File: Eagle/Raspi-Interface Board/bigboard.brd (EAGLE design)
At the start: 41.9 x 42.9 mm, 25 parts, among them M1 SMALL_SERVO, M2 SMALL_SERVO, M3 SMALL_SERVO, M4 SMALL_SERVO, M5 SMALL_SERVO, U1 ATMEGA328P-AU

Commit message: AVR ISP pins corrected
In the R1 of the board the AVR ISP pins were totally attached to the
wrong. 13 != 3. Double check work done at 4AM next time.
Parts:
- removed IC1, IC2: (no value), RepRapjr:TO92-LINE
- added 3VREG, 5VREG: (no value), SparkFun-Connectors:1X03
- added U$1, U$2: (no value), SparkFun-Aesthetics:FKIT-LOGO_VERY_SMALL
- moved R3 8.13 mm to (11.4, 11.4), turned to 180 degrees
- moved R2 7.18 mm to (11.4, 14.0)
- moved R1 6.35 mm to (11.4, 16.5)
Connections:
- net 3V: now also 3VREG.1; no longer IC2.3
- net 5V: now also 3VREG.3, 5VREG.1; no longer IC1.3, IC2.1
- net A3: now also JP3.4
- net A4: no longer JP3.4
- net ATX: no longer ISP1.1
- net D12: now also ISP1.1
- net D13: now also ISP1.3
- net D3: no longer ISP1.3
- net GND: now also 3VREG.2, 5VREG.2; no longer IC1.2, IC2.2
- net VIN: now also 5VREG.3; no longer IC1.1
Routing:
- net D12: track 42.0 -> 93.9 mm, vias 3 -> 2
- net D11: track 78.2 -> 50.3 mm, vias 1 -> 2
- net D13: track 34.8 -> 59.1 mm, vias 3 -> 1
- net A3: track 0.00 -> 23.2 mm, vias 0 -> 2
- net D3: track 31.9 -> 12.8 mm, vias 2 -> 1
- net ATX: track 38.1 -> 23.3 mm, vias 3 -> 2
- net D9: track 32.2 -> 42.8 mm
- net RRX: track 17.4 -> 9.49 mm
- net ARX: track 36.1 -> 28.3 mm, vias 2 -> 1
- net RESET: track 26.4 -> 33.4 mm
- net A2: track 29.8 -> 24.1 mm, vias 0 -> 2
- net D8: track 47.2 -> 42.5 mm, vias 4 -> 2
- net D10: track 36.1 -> 31.7 mm
- net D7: track 32.5 -> 36.6 mm, vias 1 -> 2
- net GND: track 3.19 -> 0.00 mm, vias 13 -> 2
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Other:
- board text added: "4%"
- board text added: "5/18/14"
- board text added: "R3"
- board text removed: "5/5/14"
- board text removed: "Approved"
- board text removed: "CC BY-SA 4.0"
- board text removed: "R1"

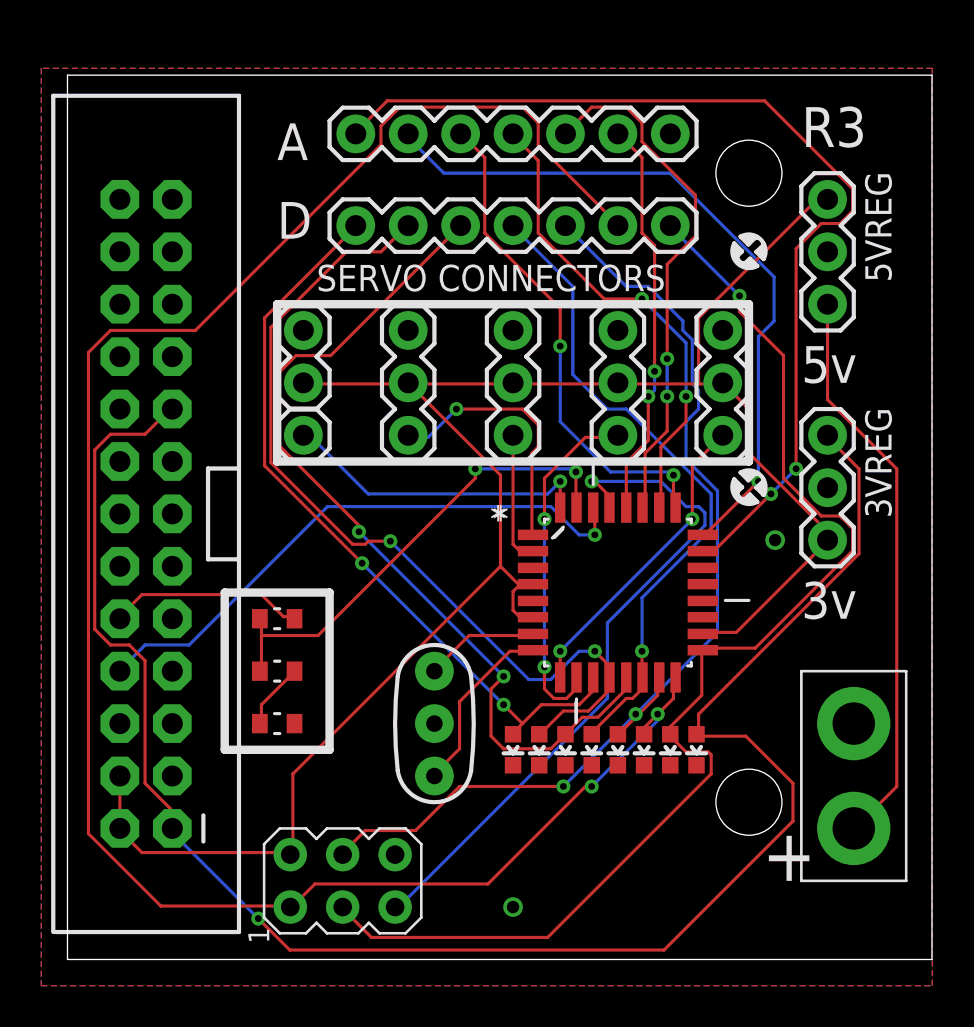
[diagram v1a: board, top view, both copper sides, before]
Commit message: Board Update
New Board revision to fix the 3v3 regulator pinout.
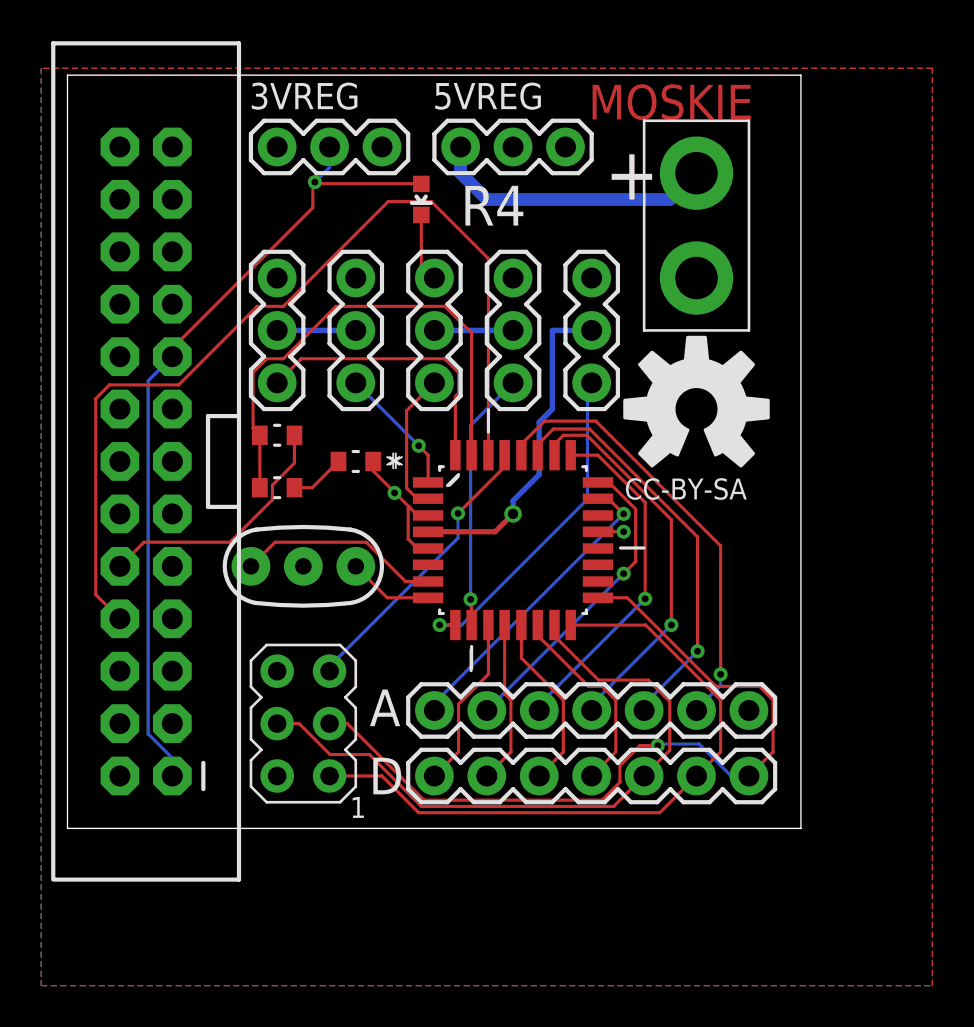
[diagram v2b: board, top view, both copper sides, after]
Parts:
- removed D1, D2, D3, D4, D5, D6, D7: BLUE, SparkFun-LED:LED-0603
- removed U$2: (no value), SparkFun-Aesthetics:FKIT-LOGO_VERY_SMALL
- U$1: device SparkFun-Aesthetics:FKIT-LOGO_VERY_SMALL -> SparkFun-Aesthetics:OSHW-LOGO-L
- moved 3VREG 30.1 mm to (11.4, 39.4), turned to 0 degrees
- moved D8 29.8 mm to (18.4, 36.8)
- moved JP3 28.2 mm to (19.1, 12.1)
- moved JP2 27.7 mm to (31.8, 35.6), turned to 270 degrees
- moved JP4 26.9 mm to (19.1, 8.89)
- moved 5VREG 18.0 mm to (20.3, 39.4), turned to 0 degrees
- moved R3 13.3 mm to (15.2, 24.1)
- moved Y1 9.92 mm to (12.7, 19.1), turned to 0 degrees
- moved R2 8.89 mm to (11.4, 22.9)
- moved R1 8.89 mm to (11.4, 25.4)
- moved U$1 8.03 mm to (31.8, 26.7)
- moved ISP1 7.85 mm to (12.7, 11.4), turned to 180 degrees
- moved M4 6.84 mm to (26.7, 27.9)
- moved M5 5.68 mm to (22.9, 27.9)
- moved U1 5.68 mm to (22.9, 20.3)
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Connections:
- net 3V: now also 3VREG.2; no longer 3VREG.1
- net 5V: now also 5VREG.3; no longer 5VREG.1
- net D10: no longer D4.A
- net D11: no longer D5.A
- net D12: no longer D6.A
- net D13: no longer D7.A
- net D7: no longer D1.A
- net D8: no longer D2.A
- net D9: no longer D3.A
- net GND: now also 3VREG.1; no longer 3VREG.2, D1.C, D2.C, D3.C, D4.C, D5.C, D6.C, D7.C
- net VIN: now also 5VREG.1; no longer 5VREG.3
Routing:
- net 5V: track 95.4 -> 23.7 mm, vias 0 -> 1
- net D12: track 93.9 -> 32.2 mm, vias 2 -> 0
- net 3V: track 86.2 -> 39.8 mm
- net D8: track 42.5 -> 7.93 mm, vias 2 -> 0
- net D9: track 42.8 -> 8.64 mm, vias 2 -> 0
- net A0: track 48.0 -> 14.9 mm, vias 2 -> 1
- net D7: track 36.6 -> 8.40 mm, vias 2 -> 0
- net D10: track 31.7 -> 9.75 mm, vias 1 -> 0
- net D13: track 59.1 -> 38.8 mm
- net A1: track 34.8 -> 15.1 mm
- net RESET: track 33.4 -> 14.0 mm
- net D11: track 50.3 -> 31.6 mm, vias 2 -> 0
- net ARX: track 28.3 -> 44.8 mm, vias 1 -> 0
- net VIN: track 27.7 -> 13.8 mm
- net GND: track 0.00 -> 11.3 mm
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- added copper zone on layer 1, net 5V
- removed copper zone on layer 1, net GND
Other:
- board size 41.9 x 42.9 mm -> 35.5 x 36.5 mm
- board text added: "CC-BY-SA"
- board text added: "MOSKIE"
- board text added: "R4"
- board text removed: "3v"
- board text removed: "4%"
- board text removed: "5/18/14"
- board text removed: "5v"
- board text removed: "Michael Moskie"
- board text removed: "R3"
- board text removed: "SERVO CONNECTORS"
